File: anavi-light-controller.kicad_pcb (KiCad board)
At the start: 2 copper layers, 74.9 x 40.6 mm, 27 parts, among them J1 Screw_Terminal_1x04, P1 CONN_01X03, Q1 IRF8721PBF-1, Q2 IRF8721PBF-1, Q3 IRF8721PBF-1, SW1 SW_DIP_x01, U1 I2C_SENS_1, U2 I2C_SENS_1, U3 I2C_SENS_1

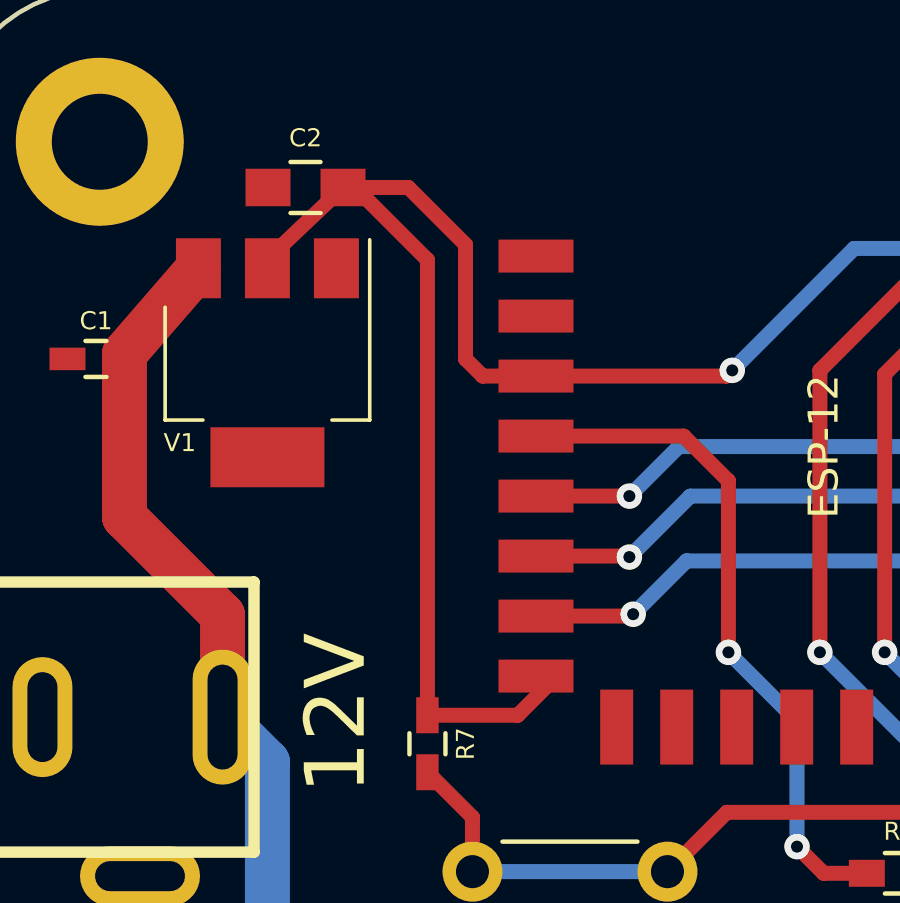
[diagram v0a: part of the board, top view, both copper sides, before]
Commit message: anavi-light-controller.kicad_pcb: Improve routing
Improve the 3.3V wiring.

Signed-off-by: Leon Anavi <leon@anavi.org>
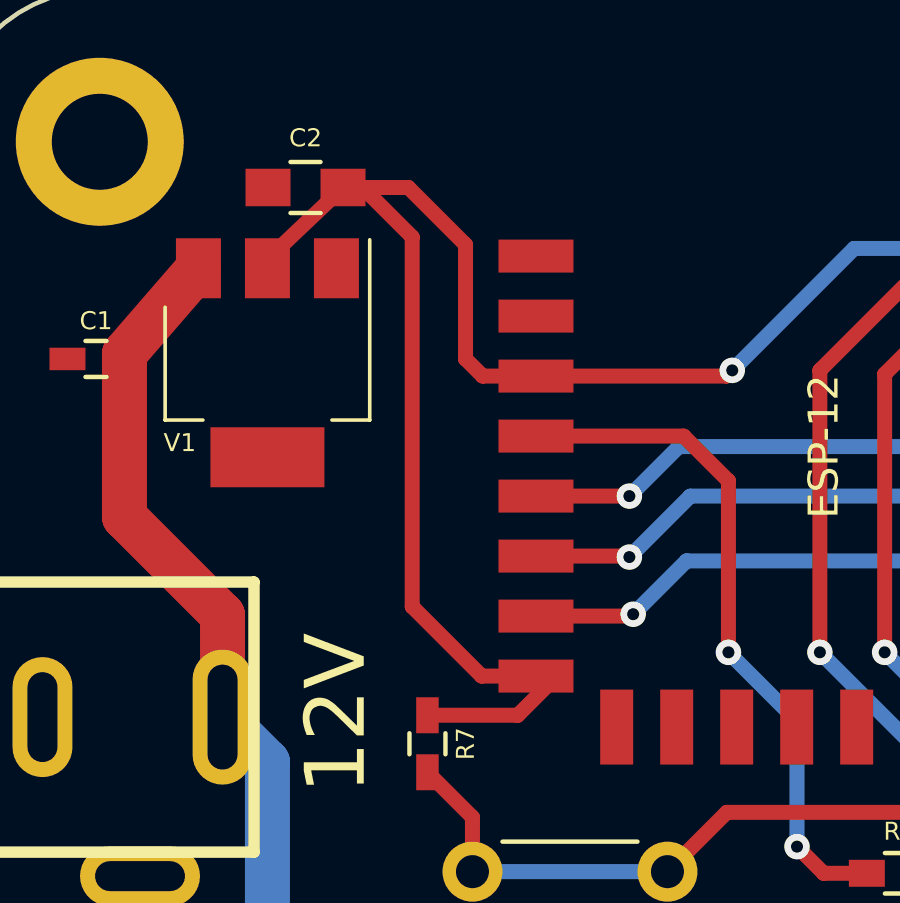
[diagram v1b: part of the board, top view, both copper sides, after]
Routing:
- net +3V3: track 95.6 -> 98.1 mm
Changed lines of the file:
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@@
     (thickness 1.6)
     (drawings 28)
-    (tracks 173)
+    (tracks 176)
     (zones 0)
     (modules 27)
@@
   (segment (start 135.175 94.06) (end 136.652 93.933) (width 1.5) (layer F.Cu) (net 5) (status 20))
   (segment (start 127.635 101.6) (end 135.175 94.06) (width 1.5) (layer F.Cu) (net 5))
+  (segment (start 80.772 95.316) (end 83.784 95.316) (width 0.5) (layer F.Cu) (net 6))
+  (segment (start 83.784 95.316) (end 85.09 94.01) (width 0.5) (layer F.Cu) (net 6))
+  (segment (start 85.09 94.01) (end 82.58 94.01) (width 0.5) (layer F.Cu) (net 6))
+  (segment (start 80.264 79.375) (end 78.613 77.724) (width 0.5) (layer F.Cu) (net 6))
+  (segment (start 80.264 91.694) (end 80.264 79.375) (width 0.5) (layer F.Cu) (net 6))
+  (segment (start 82.58 94.01) (end 80.264 91.694) (width 0.5) (layer F.Cu) (net 6))
+  (segment (start 78.613 77.724) (end 77.958 77.724) (width 0.5) (layer F.Cu) (net 6))
   (segment (start 77.958 77.724) (end 80.137 77.724) (width 0.5) (layer F.Cu) (net 6))
   (segment (start 82.613 84.01) (end 85.09 84.01) (width 0.5) (layer F.Cu) (net 6))
@@
   (segment (start 82.042 79.629) (end 82.042 83.439) (width 0.5) (layer F.Cu) (net 6))
   (segment (start 80.137 77.724) (end 82.042 79.629) (width 0.5) (layer F.Cu) (net 6))
-  (segment (start 80.772 95.316) (end 83.784 95.316) (width 0.5) (layer F.Cu) (net 6))
-  (segment (start 83.784 95.316) (end 85.09 94.01) (width 0.5) (layer F.Cu) (net 6))
   (segment (start 77.958 77.724) (end 78.359 77.724) (width 0.5) (layer F.Cu) (net 6))
-  (segment (start 78.359 77.724) (end 80.772 80.137) (width 0.5) (layer F.Cu) (net 6))
-  (segment (start 80.772 80.137) (end 80.772 95.316) (width 0.5) (layer F.Cu) (net 6))
   (segment (start 85.09 84.01) (end 90.742 84.01) (width 0.5) (layer F.Cu) (net 6))
   (segment (start 113.114 78.91) (end 113.114 78.232) (width 0.5) (layer F.Cu) (net 6))
